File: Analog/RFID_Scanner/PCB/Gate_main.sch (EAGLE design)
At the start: 14 parts

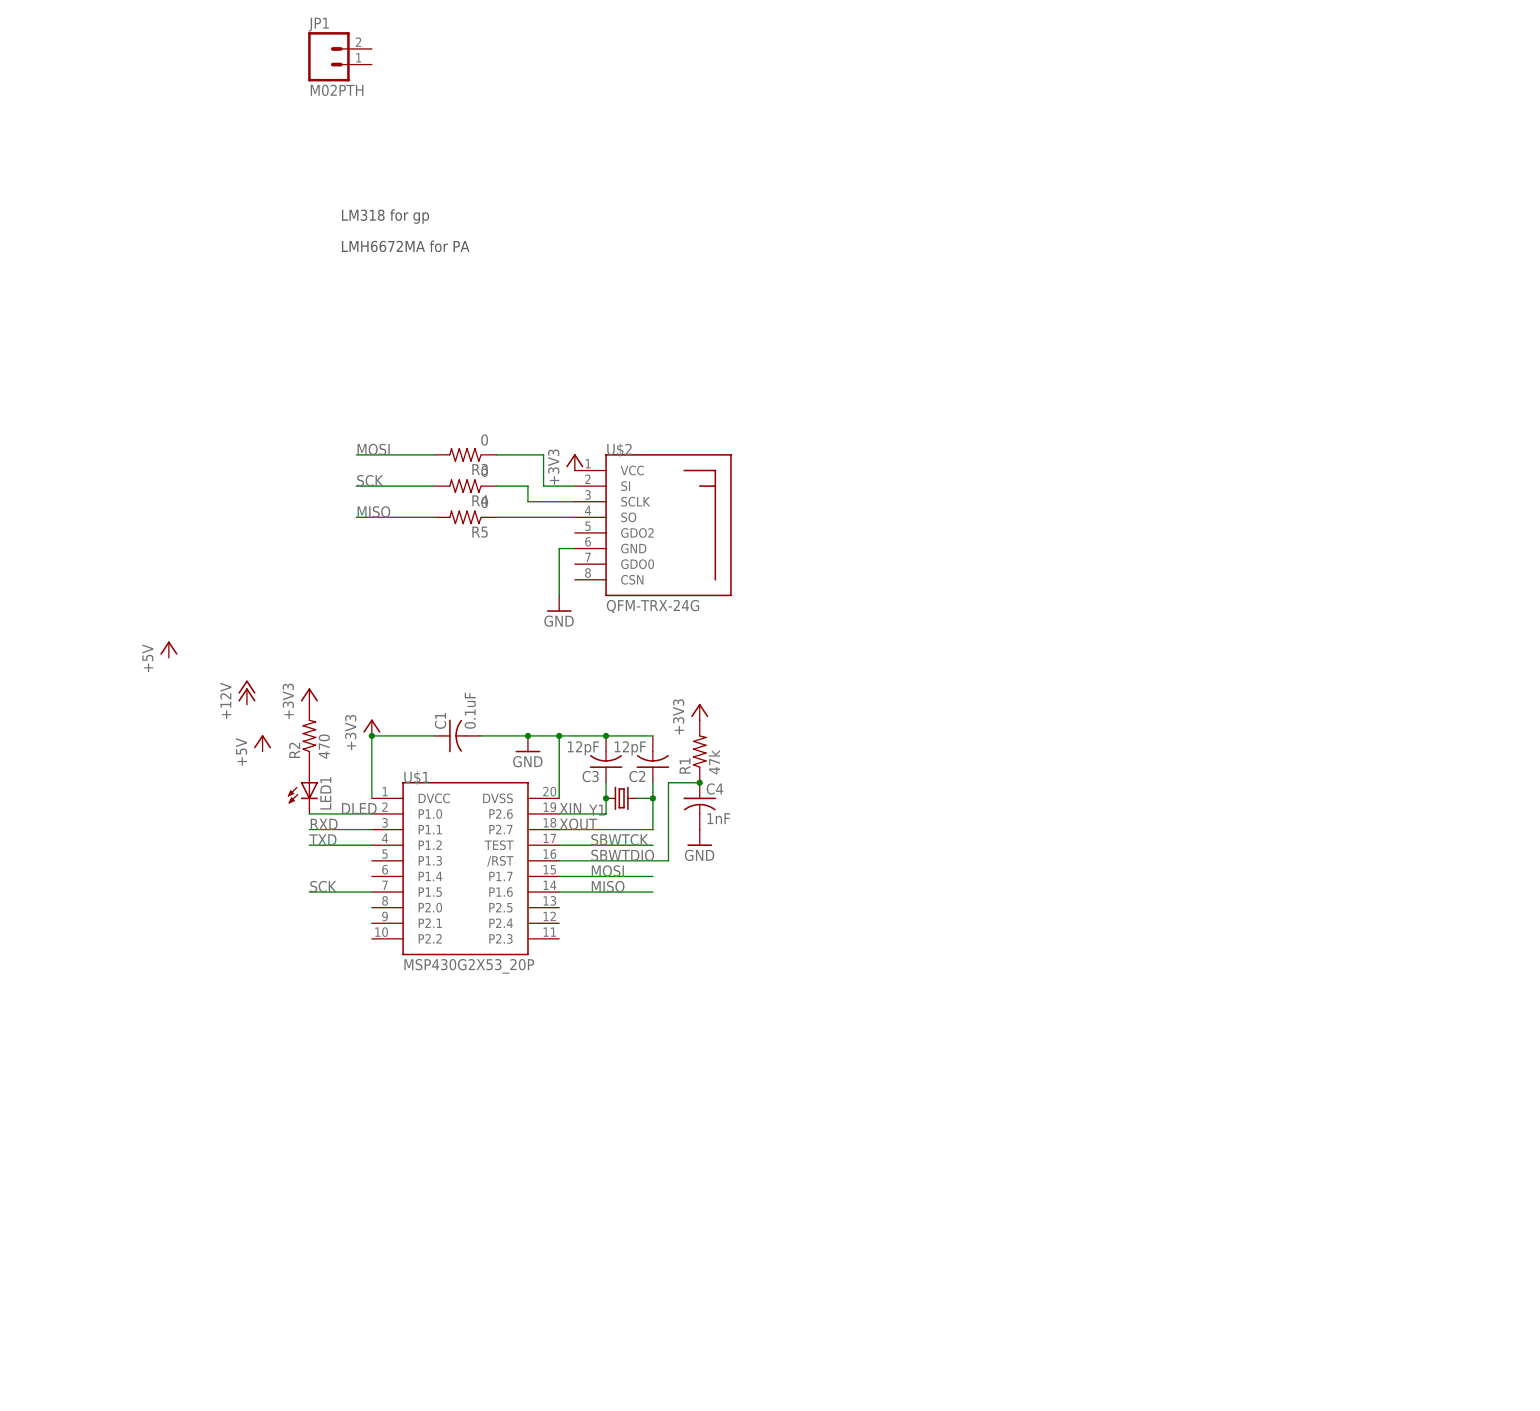
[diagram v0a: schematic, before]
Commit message: PCB and firmware
Gate PCB 70% completed, need to figure out pinout for MCU and layout
signal amps.  Board size reduced by 50%.  Also need to add testpoints
Robot PCB PSU layout completed, motor and stepper drivers will move to
separate PCB
Created firmware files, w/o code
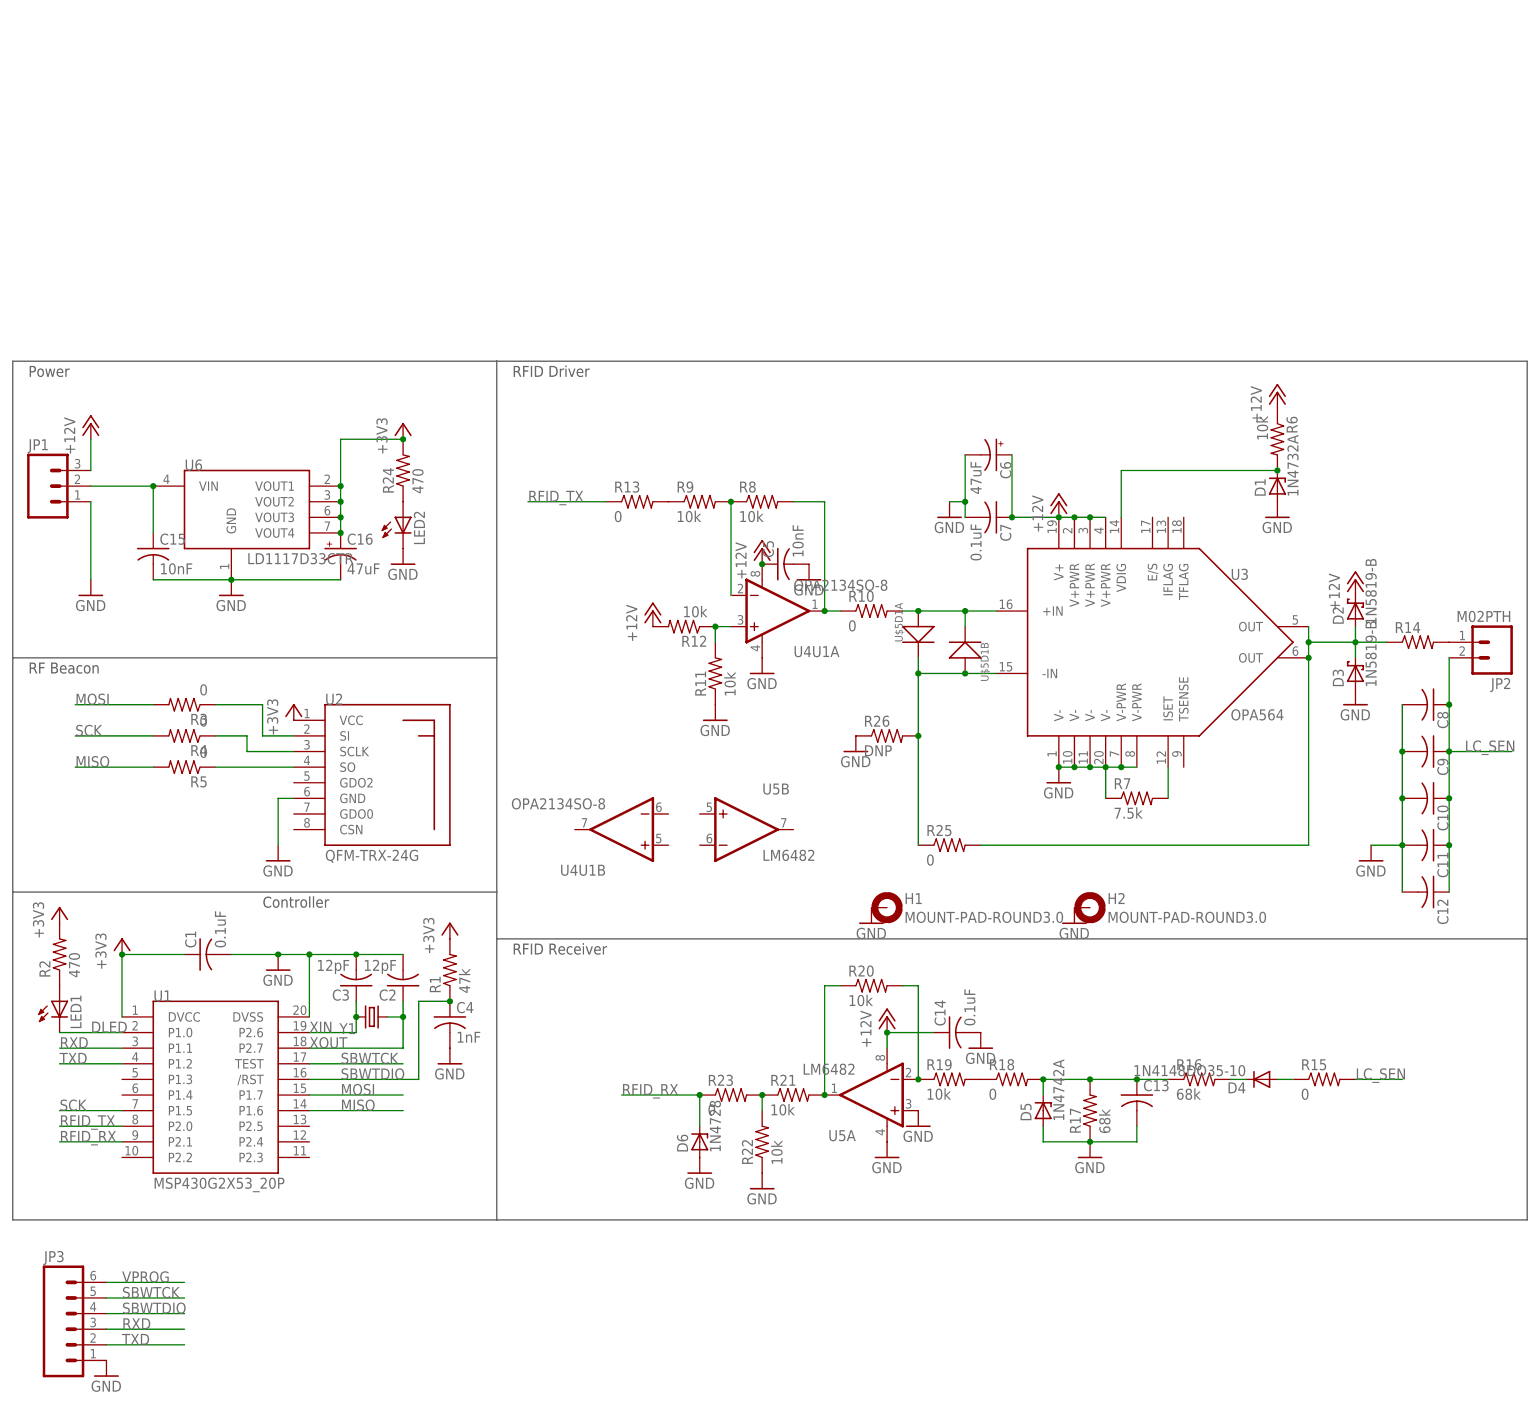
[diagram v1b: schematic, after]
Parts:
- removed U$1: MSP430G2X53_20P, npol:MSP430G2X53_20P
- removed U$2: QFM-TRX-24G, npol:QFM-TRX-24G
- added C10, C11, C12, C13, C8, C9: (no value), rcl:C-USC0805
- added C14, C7: 0.1uF, rcl:C-USC0805
- added C15, C5: 10nF, rcl:C-USC0805
- added C16, C6: 47uF, rcl:CPOL-USE2.5-6
- added D1: 1N4732A, diode:1N4728
- added D2, D3: 1N5819-B, diode:1N5819-B
- added D4: 1N4148DO35-10, diode:1N4148DO35-10
- added D5: 1N4742A, diode:1N4728
- added D6: 1N4728, diode:1N4728
- added H1, H2: MOUNT-PAD-ROUND3.0, holes:MOUNT-PAD-ROUND3.0
- added JP2: M02PTH, SparkFun-Connectors:M02PTH
- added JP3: (no value), SparkFun-Connectors:M06SIP
- added LED2: (no value), led:LEDCHIPLED_0603
- added R10, R13, R15, R18, R23, R25: 0, rcl:R-US_R0805
- added R11, R12, R19, R20, R21, R22, R6, R8, R9: 10k, rcl:R-US_R0805
- added R14: (no value), rcl:R-US_0207/10
- added R16, R17: 68k, rcl:R-US_R0805
- added R24: 470, rcl:R-US_R0805
- added R26: DNP, rcl:R-US_R0805
- added R7: 7.5k, rcl:R-US_R0805
- added U$5: SMS3922-015LF, npol:SMS3922-015LF
- added U1: MSP430G2X53_20P, npol:MSP430G2X53_20P
- added U2: QFM-TRX-24G, npol:QFM-TRX-24G
- added U3: OPA564, npol:OPA564
- added U4: OPA2134SO-8, npol:OPA2134SO-8
- added U5: LM6482, npol:LM6482
- added U6: LD1117D33CTR, npol:LD1117D33CTR
- JP1: value M02PTH -> (none); device SparkFun-Connectors:M02PTH -> SparkFun-Connectors:M03PTH
- LED1: device led:LEDCHIP-LED0805 -> led:LEDCHIPLED_0603
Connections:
- new net +12V: C14.1, C5.1, C6.+, C7.1, D2.C, JP1.3, R12.2, R6.1, U3.V+, U3.V+PWR@2, U3.V+PWR@3, U3.V+PWR@4, U4U1A.V+, U5A.V+
- new net +6V: C15.1, JP1.2, U6.VIN
- new net BIAS_OUT: R10.1, R8.2, U4U1A.OUT
- new net ISET: R7.2, U3.ISET
- new net LC_SEN: C10.1, C11.1, C12.1, C8.1, C9.1, JP2.2, R15.2
- new net N$10: D4.C, R16.2
- new net N$11: D4.A, R15.1
- new net N$12: R25.1, R26.2, U$5D1A.K, U$5D1B.A, U3.-IN
- new net N$13: C13.1, D5.C, R16.1, R17.2, R18.2
- new net N$14: R18.1, R19.2
- new net N$15: R19.1, R20.2, U5A.-IN
- new net N$16: R20.1, R21.2, U5A.OUT
- new net N$17: R21.1, R22.2, R23.2
- new net N$19: LED2.A, R24.1
- new net N$5: R8.1, R9.2, U4U1A.-IN
- new net N$6: R10.2, U$5D1A.A, U$5D1B.K, U3.+IN
- new net N$7: R11.2, R12.1, U4U1A.+IN
- new net N$8: R13.2, R9.1
- new net N$9: JP2.1, R14.2
- new net PA_OUT: D2.A, D3.C, R14.1, R25.2, U3.OUT@5, U3.OUT@6
- new net RFID_RX: D6.C, R23.1, U1.P2.1
- new net RFID_TX: R13.1, U1.P2.0
- new net VDIG: D1.C, R6.2, U3.VDIG
- new net VPROG: JP3.6
- net +3V3: now also C16.+, R24.2, U1.DVCC, U2.VCC, U6.VOUT1, U6.VOUT2, U6.VOUT3, U6.VOUT4; no longer U$1.DVCC, U$2.VCC
- net DLED: now also U1.P1.0; no longer U$1.P1.0
- net GND: now also C10.2, C11.2, C12.2, C13.2, C14.2, C15.2, C16.-, C5.2, C6.-, C7.2, C8.2, C9.2, D1.A, D3.A, D5.A, D6.A, H1.MOUNT, H2.MOUNT, JP1.1, JP3.1, LED2.C, R11.1, R17.1, R22.1, R26.1, R7.1, U1.DVSS, U2.GND, U3.V-@1, U3.V-@10, U3.V-@11, U3.V-@20, U3.V-PWR@7, U3.V-PWR@8, U4U1A.V-, U5A.+IN, U5A.V-, U6.GND; no longer U$1.DVSS, U$2.GND
- net MISO: now also U1.P1.6; no longer U$1.P1.6
- net MOSI: now also U1.P1.7; no longer U$1.P1.7
- net N$2: now also U2.SO; no longer U$2.SO
- net N$3: now also U2.SCLK; no longer U$2.SCLK
- net N$4: now also U2.SI; no longer U$2.SI
- net RXD: now also JP3.3, U1.P1.1; no longer U$1.P1.1
- net SBWTCK: now also JP3.5, U1.TEST; no longer U$1.TEST
- net SBWTDIO: now also JP3.4, U1./RST; no longer U$1./RST
- net SCK: now also U1.P1.5; no longer U$1.P1.5
- net TXD: now also JP3.2, U1.P1.2; no longer U$1.P1.2
- net XIN: now also U1.P2.6; no longer U$1.P2.6
- net XOUT: now also U1.P2.7; no longer U$1.P2.7
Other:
- note added: "Controller"
- note added: "Power"
- note added: "RF Beacon"
- note added: "RFID Driver"
- note added: "RFID Receiver"
- note removed: "BATT"
- note removed: "LM318 for gp"
- note removed: "LMH6672MA for PA"
- moved on the sheet: C1, C2, C3, C4, LED1, R1, R2, R3, R4, R5, Y1

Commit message: Gate PCB progress
Did layout for gate pcb signal amps, finalized board size, added
testpoints
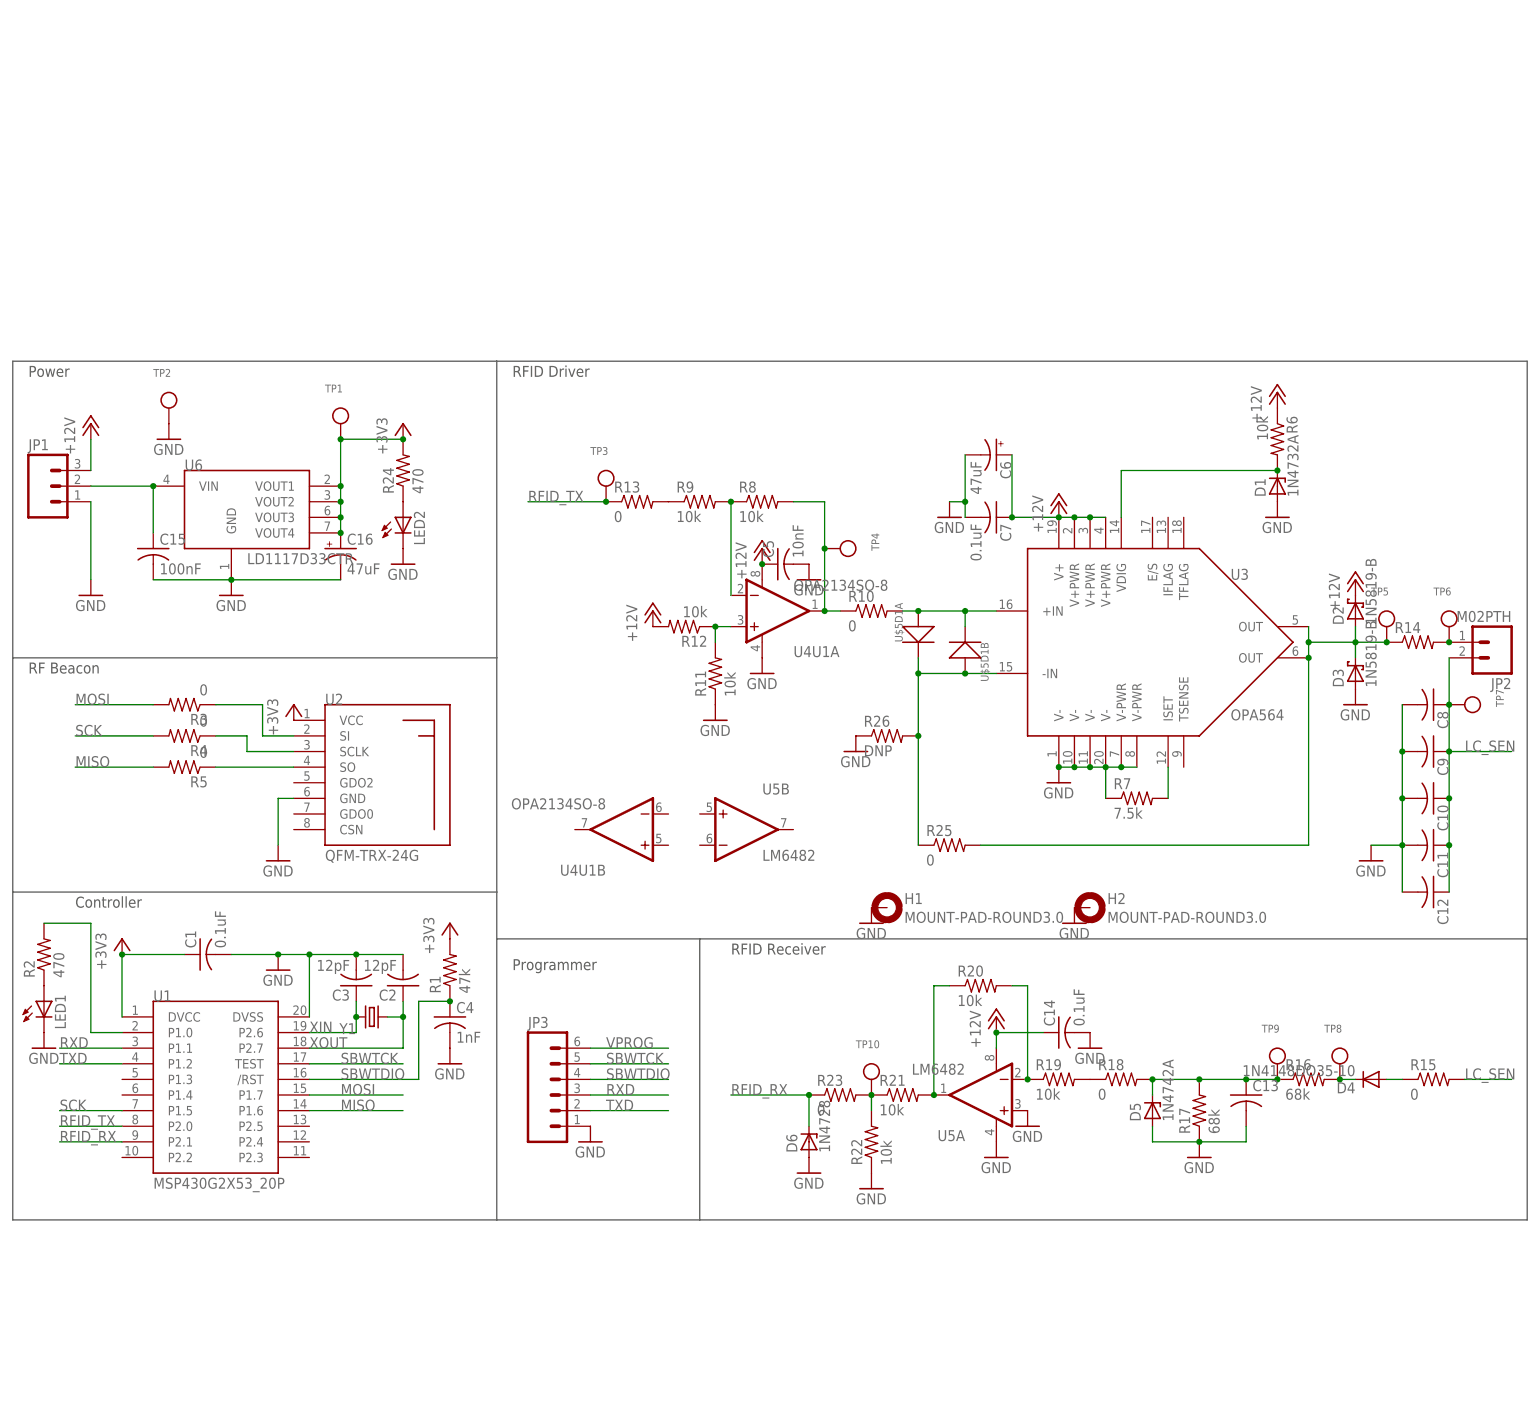
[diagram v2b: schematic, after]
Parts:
- added TP1, TP10, TP2, TP3, TP4, TP5, TP6, TP7, TP8, TP9: (no value), microbuilder:TESTPOINT0.1"
- C15: value 10nF -> 100nF
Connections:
- removed net DLED: LED1.C, U1.P1.0
- new net N$18: R2.2, U1.P1.0
- net +3V3: now also TP1.P$1; no longer R2.2
- net BIAS_OUT: now also TP4.P$1
- net GND: now also LED1.C, TP2.P$1
- net LC_SEN: now also TP7.P$1
- net N$10: now also TP8.P$1
- net N$13: now also TP9.P$1
- net N$17: now also TP10.P$1
- net N$9: now also TP6.P$1
- net PA_OUT: now also TP5.P$1
- net RFID_TX: now also TP3.P$1
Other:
- note added: "Programmer"
- note removed: "MCP1700-3.3 LDO"
- moved on the sheet: C13, C14, D4, D5, D6, JP3, LED1, R15, R16, R17, R18, R19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

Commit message: Board final; SPI progress
Sent PCBs to FAB
SPI driver working for multi-byte.  Bug: bytes are sent in reversed
order, although bit ordering (MSB first) is correct.
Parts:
- added JP4: (no value), SparkFun-Connectors:M03X22X3_SILK_SM
- added R27, R28, R29: 0, rcl:R-US_R0805
- added R30, R31, R32: 10k, rcl:R-US_R0805
- added TP11: (no value), microbuilder:TESTPOINT0.1"
- C13: value (none) -> 6.8n
- R11: value 10k -> 12k
- R12, R21: value 10k -> 33k
- R19: value 10k -> 0
- R20: value 10k -> DNP
- R8: value 10k -> 15k
- R9: value 10k -> 8.2k
- U1: value MSP430G2X53_20P -> MSP430G2X53_20PPW; device npol:MSP430G2X53_20P -> npol:MSP430G2X53_20PPW
- Y1: value (none) -> 8MHz
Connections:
- removed net N$14 (its old number): R18.1, R19.2
- new net CS: R29.2, U1.P1.4
- new net GDO0: R28.2, U1.P2.0
- new net GDO2: R27.2, U1.P2.2
- new net ID0: JP4.2, R30.1, U1.P2.3
- new net ID1: JP4.4, R31.1, U1.P2.4
- new net ID2: JP4.6, R32.1, U1.P2.5
- new net N$15: R19.2, R21.1, U5A.OUT
- new net N$20: R29.1, U2.CSN
- new net N$21: R28.1, U2.GDO0
- new net N$22: R27.1, U2.GDO2
- net +3V3: now also R30.2, R31.2, R32.2
- net GND: now also JP4.1, JP4.3, JP4.5, R20.1; no longer U5A.+IN
- net N$16: now also R18.1, U5A.+IN; no longer R20.1, R21.2, U5A.OUT
- net N$17: now also R21.2; no longer R21.1
- net N$8: now also TP11.P$1
- net RFID_RX: now also U1.P1.3; no longer U1.P2.1
- net RFID_TX: now also U1.P2.1; no longer U1.P2.0
- net RXD: now also JP3.5; no longer JP3.3
- net SBWTCK: now also JP3.3; no longer JP3.5
- net TXD: now also JP3.6; no longer JP3.2
- net VPROG: now also JP3.2; no longer JP3.6
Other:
- moved on the sheet: JP3, R19, R20, R21, R3, R4, U4U1B, U5B
